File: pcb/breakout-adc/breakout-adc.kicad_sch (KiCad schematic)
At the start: 26 parts, among them J1 Screw_Terminal_01x04, J10 Conn_01x01_Pin, J11 Conn_01x12_Pin, J12 Conn_01x12_Pin, J13 Conn_01x01_Pin, J14 Conn_01x01_Pin, J15 FX18-120P-0.8SV20, J16 Conn_01x01_Pin, J17 Conn_01x01_Pin, J18 Conn_01x01_Pin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

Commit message: [adc][pcb] add colored keystone tp fp and models
Note: these need to have their footprints and models fixed
as they get used. I only did the ones on this board, even
though I downloaded and committed all the colors.
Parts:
- J7: footprint TestPoint:TestPoint_Keystone_5000-5004_Miniature -> keystone:KEYSTONE_5000
- J8: footprint TestPoint:TestPoint_Keystone_5000-5004_Miniature -> keystone:KEYSTONE_5116
- J9: footprint TestPoint:TestPoint_Keystone_5000-5004_Miniature -> keystone:KEYSTONE_5117
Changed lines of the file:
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@@
 			)
 		)
-		(property "Footprint" "TestPoint:TestPoint_Keystone_5000-5004_Miniature"
+		(property "Footprint" "keystone:KEYSTONE_5117"
 			(at 298.45 92.71 0)
 			(effects
@@
 			)
 		)
-		(property "Footprint" "TestPoint:TestPoint_Keystone_5000-5004_Miniature"
+		(property "Footprint" "keystone:KEYSTONE_5000"
 			(at 298.45 85.09 0)
 			(effects
@@
 			)
 		)
-		(property "Footprint" "TestPoint:TestPoint_Keystone_5000-5004_Miniature"
+		(property "Footprint" "keystone:KEYSTONE_5116"
 			(at 298.45 88.9 0)
 			(effects

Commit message: [adc][pcb] move the 3v3 and gnd tp to the edge
This will (probably) allow for grabbers to connect
to the through holes even if the tp isn't soldered in.
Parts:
- J10, J14, J16, J17, J18, J5, J6: footprint TestPoint:TestPoint_Keystone_5000-5004_Miniature -> keystone:KEYSTONE_5001
- J13: footprint TestPoint:TestPoint_Keystone_5000-5004_Miniature -> keystone:KEYSTONE_5000
- J3, J4: footprint TestPoint:TestPoint_Keystone_5000-5004_Miniature -> keystone:KEYSTONE_5002
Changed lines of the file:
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@@
 			)
 		)
-		(property "Footprint" "TestPoint:TestPoint_Keystone_5000-5004_Miniature"
+		(property "Footprint" "keystone:KEYSTONE_5001"
 			(at 392.43 63.5 0)
 			(effects
@@
 			)
 		)
-		(property "Footprint" "TestPoint:TestPoint_Keystone_5000-5004_Miniature"
+		(property "Footprint" "keystone:KEYSTONE_5002"
 			(at 298.45 58.42 0)
 			(effects
@@
 			)
 		)
-		(property "Footprint" "TestPoint:TestPoint_Keystone_5000-5004_Miniature"
+		(property "Footprint" "keystone:KEYSTONE_5002"
 			(at 298.45 55.88 0)
 			(effects
@@
 			)
 		)
-		(property "Footprint" "TestPoint:TestPoint_Keystone_5000-5004_Miniature"
+		(property "Footprint" "keystone:KEYSTONE_5001"
 			(at 298.45 96.52 0)
 			(effects
@@
 			)
 		)
-		(property "Footprint" "TestPoint:TestPoint_Keystone_5000-5004_Miniature"
+		(property "Footprint" "keystone:KEYSTONE_5001"
 			(at 392.43 90.17 0)
 			(effects
@@
 			)
 		)
-		(property "Footprint" "TestPoint:TestPoint_Keystone_5000-5004_Miniature"
+		(property "Footprint" "keystone:KEYSTONE_5001"
 			(at 392.43 85.09 0)
 			(effects
@@
 			)
 		)
-		(property "Footprint" "TestPoint:TestPoint_Keystone_5000-5004_Miniature"
+		(property "Footprint" "keystone:KEYSTONE_5001"
 			(at 392.43 87.63 0)
 			(effects
@@
 			)
 		)
-		(property "Footprint" "TestPoint:TestPoint_Keystone_5000-5004_Miniature"
+		(property "Footprint" "keystone:KEYSTONE_5001"
 			(at 298.45 63.5 0)
 			(effects
@@
 			)
 		)
-		(property "Footprint" "TestPoint:TestPoint_Keystone_5000-5004_Miniature"
+		(property "Footprint" "keystone:KEYSTONE_5000"
 			(at 392.43 60.96 0)
 			(effects
@@
 			)
 		)
-		(property "Footprint" "TestPoint:TestPoint_Keystone_5000-5004_Miniature"
+		(property "Footprint" "keystone:KEYSTONE_5001"
 			(at 298.45 60.96 0)
 			(effects

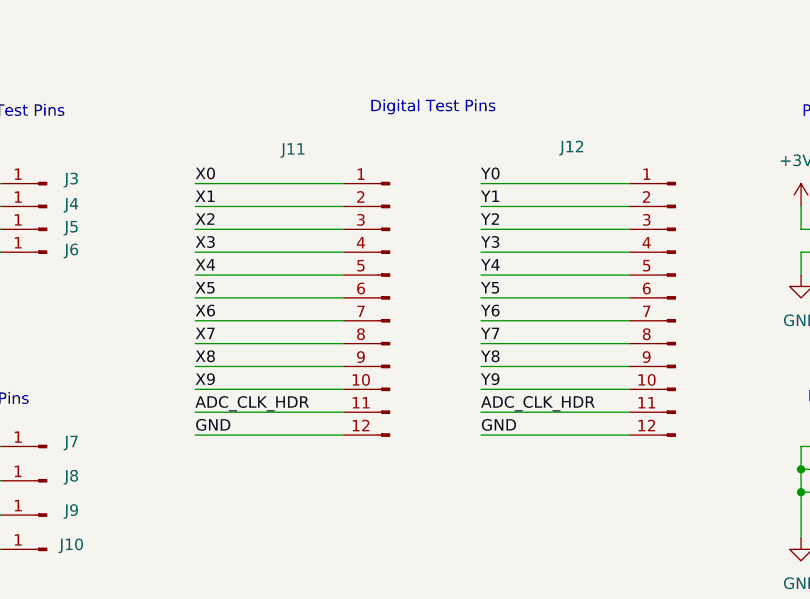
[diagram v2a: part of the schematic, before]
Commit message: [adc][pcb] routed data to buffers
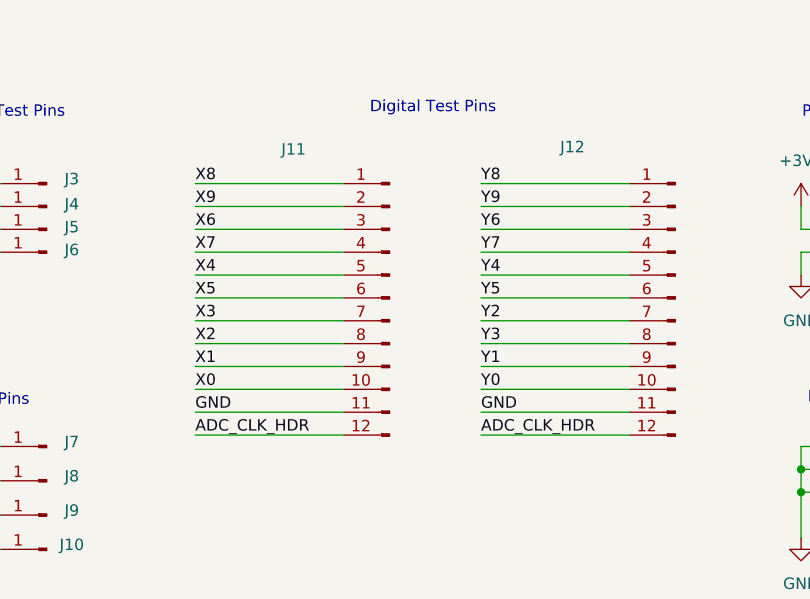
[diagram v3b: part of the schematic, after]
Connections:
- net ADC_CLK_HDR: now also J11.12 (Pin_12), J12.12 (Pin_12); no longer J11.11 (Pin_11), J12.11 (Pin_11)
- net GND: now also J11.11 (Pin_11), J12.11 (Pin_11); no longer J11.12 (Pin_12), J12.12 (Pin_12)
- net X0: now also J11.10 (Pin_10); no longer J11.1 (Pin_1)
- net X1: now also J11.9 (Pin_9); no longer J11.2 (Pin_2)
- net X2: now also J11.8 (Pin_8); no longer J11.3 (Pin_3)
- net X3: now also J11.7 (Pin_7); no longer J11.4 (Pin_4)
- net X6: now also J11.3 (Pin_3); no longer J11.7 (Pin_7)
- net X7: now also J11.4 (Pin_4); no longer J11.8 (Pin_8)
- net X8: now also J11.1 (Pin_1); no longer J11.9 (Pin_9)
- net X9: now also J11.2 (Pin_2); no longer J11.10 (Pin_10)
- net Y0: now also J12.10 (Pin_10); no longer J12.1 (Pin_1)
- net Y1: now also J12.9 (Pin_9); no longer J12.2 (Pin_2)
- net Y2: now also J12.7 (Pin_7); no longer J12.3 (Pin_3)
- net Y3: now also J12.8 (Pin_8); no longer J12.4 (Pin_4)
- net Y6: now also J12.3 (Pin_3); no longer J12.7 (Pin_7)
- net Y7: now also J12.4 (Pin_4); no longer J12.8 (Pin_8)
- net Y8: now also J12.1 (Pin_1); no longer J12.9 (Pin_9)
- net Y9: now also J12.2 (Pin_2); no longer J12.10 (Pin_10)
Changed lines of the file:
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@@
 	)
 	(label "Y0"
-		(at 346.71 55.88 0)
+		(at 346.71 78.74 0)
 		(fields_autoplaced yes)
 		(effects
@@
 	)
 	(label "GND"
-		(at 314.96 83.82 0)
+		(at 314.96 81.28 0)
 		(fields_autoplaced yes)
 		(effects
@@
 	)
 	(label "Y8"
-		(at 346.71 76.2 0)
+		(at 346.71 55.88 0)
 		(fields_autoplaced yes)
 		(effects
@@
 	)
 	(label "Y7"
+		(at 346.71 63.5 0)
+		(fields_autoplaced yes)
+		(effects
+			(font
+				(size 1.27 1.27)
+			)
+			(justify left bottom)
+		)
+	)
+	(label "GND"
+		(at 129.54 228.6 180)
+		(fields_autoplaced yes)
+		(effects
+			(font
+				(size 1.27 1.27)
+			)
+			(justify right bottom)
+		)
+	)
+	(label "Y3"
 		(at 346.71 73.66 0)
-		(fields_autoplaced yes)
-		(effects
-			(font
-				(size 1.27 1.27)
-			)
-			(justify left bottom)
-		)
-	)
-	(label "GND"
-		(at 129.54 228.6 180)
-		(fields_autoplaced yes)
-		(effects
-			(font
-				(size 1.27 1.27)
-			)
-			(justify right bottom)
-		)
-	)
-	(label "Y3"
-		(at 346.71 63.5 0)
 		(fields_autoplaced yes)
 		(effects
@@
 	)
 	(label "Y6"
-		(at 346.71 71.12 0)
+		(at 346.71 60.96 0)
 		(fields_autoplaced yes)
 		(effects
@@
 	)
 	(label "Y9"
-		(at 346.71 78.74 0)
+		(at 346.71 58.42 0)
 		(fields_autoplaced yes)
 		(effects
@@
 	)
 	(label "ADC_CLK_HDR"
-		(at 346.71 81.28 0)
+		(at 346.71 83.82 0)
 		(fields_autoplaced yes)
 		(effects
@@
 	)
 	(label "X1"
-		(at 314.96 58.42 0)
+		(at 314.96 76.2 0)
 		(fields_autoplaced yes)
 		(effects
@@
 	)
 	(label "Y1"
-		(at 346.71 58.42 0)
+		(at 346.71 76.2 0)
 		(fields_autoplaced yes)
 		(effects
@@
 	)
 	(label "X8"
-		(at 314.96 76.2 0)
+		(at 314.96 55.88 0)
 		(fields_autoplaced yes)
 		(effects
@@
 	)
 	(label "X0"
-		(at 314.96 55.88 0)
+		(at 314.96 78.74 0)
 		(fields_autoplaced yes)
 		(effects
@@
 	)
 	(label "ADC_CLK_HDR"
-		(at 314.96 81.28 0)
+		(at 314.96 83.82 0)
 		(fields_autoplaced yes)
 		(effects
@@
 	)
 	(label "X2"
-		(at 314.96 60.96 0)
+		(at 314.96 73.66 0)
 		(fields_autoplaced yes)
 		(effects
@@
 	)
 	(label "X3"
-		(at 314.96 63.5 0)
+		(at 314.96 71.12 0)
 		(fields_autoplaced yes)
 		(effects
@@
 	)
 	(label "GND"
-		(at 346.71 83.82 0)
+		(at 346.71 81.28 0)
 		(fields_autoplaced yes)
 		(effects
@@
 	)
 	(label "X9"
-		(at 314.96 78.74 0)
+		(at 314.96 58.42 0)
 		(fields_autoplaced yes)
 		(effects
@@
 	)
 	(label "Y2"
-		(at 346.71 60.96 0)
+		(at 346.71 71.12 0)
 		(fields_autoplaced yes)
 		(effects
@@
 	)
 	(label "X7"
-		(at 314.96 73.66 0)
+		(at 314.96 63.5 0)
 		(fields_autoplaced yes)
 		(effects
@@
 	)
 	(label "X6"
-		(at 314.96 71.12 0)
-		(fields_autoplaced yes)
-		(effects
+		(at 314.96 60.96 0)
+		(fields_autoplaced yes)
+		(effects

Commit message: [pcb] prep work for FX18-120P footprint fix
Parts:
- J15: footprint custom:CUSTOM_FX_120S-0.8SH20 -> CONN_120P-0.8SV20
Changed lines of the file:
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@@
 	)
 	(symbol
+		(lib_name "FX18-120P-0.8SV20_1")
 		(lib_id "FX18-120P-0-8SV20:FX18-120P-0.8SV20")
 		(at 52.07 142.24 0)
@@
 			)
 		)
-		(property "Footprint" "custom:CUSTOM_FX_120S-0.8SH20"
+		(property "Footprint" "CONN_120P-0.8SV20"
 			(at 52.07 142.24 0)
 			(effects
@@
 			)
 		)
-		(property "Datasheet" "FX18-120P-0.8SV20"
+		(property "Datasheet" "https://www.hirose.com/en/product/document?clcode=CL0579-0020-7-00&productname=FX18-120P-0.8SV&series=FX18&documenttype=2DDrawing&lang=en&documentid=0000920405"
 			(at 52.07 142.24 0)
 			(effects

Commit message: [pcb] add FX18-120P footprint and update pcbs
and a few adc fixes, including a key resistor fix
(the op amp for Y had a copy paste error from X
on the positive Rg)
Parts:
- J15: footprint custom:CUSTOM_FX_120S-0.8SH20 -> custom:CUSTOM_FX_120P-0.8SH20
- J15: footprint CONN_120P-0.8SV20 -> custom:CUSTOM_FX_120P-0.8SH20
- U8, U9: footprint D1213A:SOT-363_DIO -> SOT-363_DIO
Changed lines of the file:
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@@
 			)
 		)
-		(property "Footprint" "custom:CUSTOM_FX_120S-0.8SH20"
+		(property "Footprint" "custom:CUSTOM_FX_120P-0.8SH20"
 			(at 86.36 142.24 0)
 			(effects
@@
 			)
 		)
-		(property "Datasheet" "FX18-120P-0.8SV20"
+		(property "Datasheet" "https://www.hirose.com/en/product/document?clcode=CL0579-0020-7-00&productname=FX18-120P-0.8SV&series=FX18&documenttype=2DDrawing&lang=en&documentid=0000920405"
 			(at 86.36 142.24 0)
 			(effects
@@
 	)
 	(symbol
-		(lib_name "D1213A-04S-7_1")
 		(lib_id "D1213A-04S:D1213A-04S-7")
 		(at 111.76 46.99 0)
@@
 			)
 		)
-		(property "Footprint" "D1213A:SOT-363_DIO"
+		(property "Footprint" "SOT-363_DIO"
 			(at 111.76 46.99 0)
 			(effects
@@
 			)
 		)
-		(property "Datasheet" "https://www.diodes.com/assets/Datasheets/D1213A-04S.pdf"
+		(property "Datasheet" "D1213A-04S-7"
 			(at 111.76 46.99 0)
 			(effects
@@
 			)
 		)
-		(property "Footprint" "custom:CUSTOM_FX_120S-0.8SH20"
+		(property "Footprint" "custom:CUSTOM_FX_120P-0.8SH20"
 			(at 123.19 142.24 0)
 			(effects
@@
 			)
 		)
-		(property "Datasheet" "FX18-120P-0.8SV20"
+		(property "Datasheet" "https://www.hirose.com/en/product/document?clcode=CL0579-0020-7-00&productname=FX18-120P-0.8SV&series=FX18&documenttype=2DDrawing&lang=en&documentid=0000920405"
 			(at 123.19 142.24 0)
 			(effects
@@
 			)
 		)
-		(property "Footprint" "D1213A:SOT-363_DIO"
+		(property "Footprint" "SOT-363_DIO"
 			(at 111.76 97.79 0)
 			(effects
@@
 			)
 		)
-		(property "Datasheet" "https://www.diodes.com/assets/Datasheets/D1213A-04S.pdf"
+		(property "Datasheet" "D1213A-04S-7"
 			(at 111.76 97.79 0)
 			(effects
@@
 	)
 	(symbol
-		(lib_name "FX18-120P-0.8SV20_1")
 		(lib_id "FX18-120P-0-8SV20:FX18-120P-0.8SV20")
 		(at 52.07 142.24 0)
@@
 			)
 		)
-		(property "Footprint" "CONN_120P-0.8SV20"
+		(property "Footprint" "custom:CUSTOM_FX_120P-0.8SH20"
 			(at 52.07 142.24 0)
 			(effects

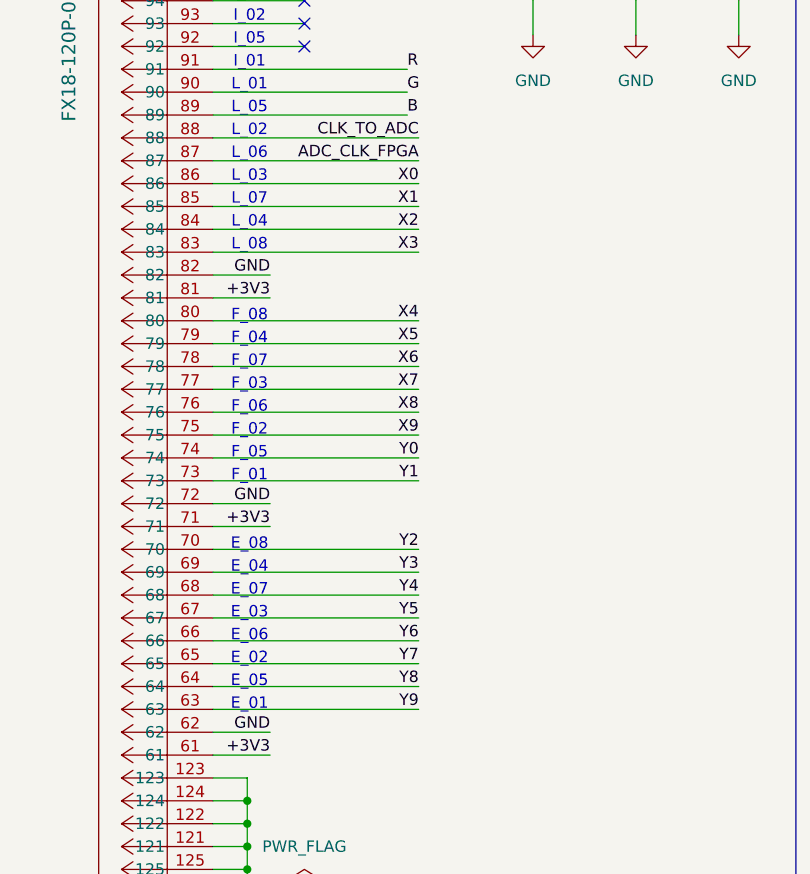
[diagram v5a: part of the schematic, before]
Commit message: [adc][pcb] data routed to FX conn
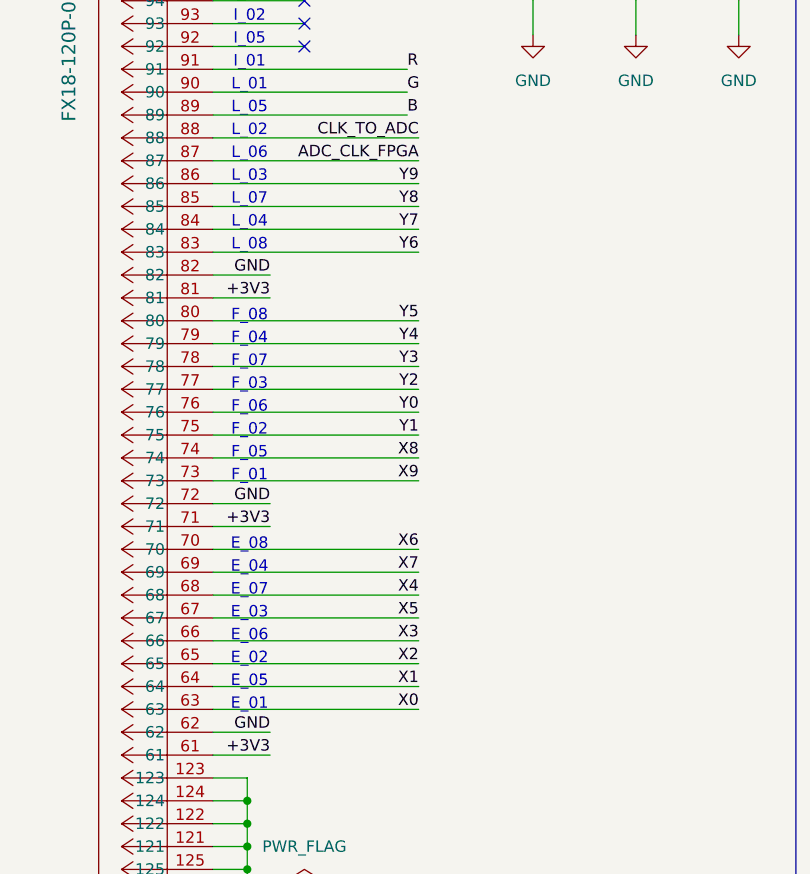
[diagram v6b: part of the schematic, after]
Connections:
- net X0: now also J15.63; no longer J15.86
- net X1: now also J15.64; no longer J15.85
- net X2: now also J15.65; no longer J15.84
- net X3: now also J15.66; no longer J15.83
- net X4: now also J15.68; no longer J15.80
- net X5: now also J15.67; no longer J15.79
- net X6: now also J15.70; no longer J15.78
- net X7: now also J15.69; no longer J15.77
- net X8: now also J15.74; no longer J15.76
- net X9: now also J15.73; no longer J15.75
- net Y0: now also J15.76; no longer J15.74
- net Y1: now also J15.75; no longer J15.73
- net Y2: now also J15.77; no longer J15.70
- net Y3: now also J15.78; no longer J15.69
- net Y4: now also J15.79; no longer J15.68
- net Y5: now also J15.80; no longer J15.67
- net Y6: now also J15.83; no longer J15.66
- net Y7: now also J15.84; no longer J15.65
- net Y8: now also J15.85; no longer J15.64
- net Y9: now also J15.86; no longer J15.63
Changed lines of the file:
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@@
 	)
 	(label "Y4"
-		(at 146.05 213.36 180)
+		(at 146.05 185.42 180)
 		(fields_autoplaced yes)
 		(effects
@@
 	)
 	(label "Y7"
-		(at 146.05 220.98 180)
+		(at 146.05 172.72 180)
 		(fields_autoplaced yes)
 		(effects
@@
 	)
 	(label "Y3"
-		(at 146.05 210.82 180)
+		(at 146.05 187.96 180)
 		(fields_autoplaced yes)
 		(effects
@@
 	)
 	(label "X8"
-		(at 146.05 193.04 180)
+		(at 146.05 198.12 180)
 		(fields_autoplaced yes)
 		(effects
@@
 	)
 	(label "Y5"
-		(at 146.05 215.9 180)
+		(at 146.05 182.88 180)
 		(fields_autoplaced yes)
 		(effects
@@
 	)
 	(label "X3"
-		(at 146.05 175.26 180)
+		(at 146.05 218.44 180)
 		(fields_autoplaced yes)
 		(effects
@@
 	)
 	(label "Y1"
-		(at 146.05 200.66 180)
+		(at 146.05 195.58 180)
 		(fields_autoplaced yes)
 		(effects
@@
 	)
 	(label "X7"
+		(at 146.05 210.82 180)
+		(fields_autoplaced yes)
+		(effects
+			(font
+				(size 1.27 1.27)
+			)
+			(justify right bottom)
+		)
+	)
+	(label "Y2"
 		(at 146.05 190.5 180)
 		(fields_autoplaced yes)
@@
 		)
 	)
-	(label "Y2"
-		(at 146.05 208.28 180)
-		(fields_autoplaced yes)
-		(effects
-			(font
-				(size 1.27 1.27)
-			)
-			(justify right bottom)
-		)
-	)
 	(label "+3V3"
 		(at 62.23 167.64 180)
@@
 	)
 	(label "X9"
-		(at 146.05 195.58 180)
+		(at 146.05 200.66 180)
 		(fields_autoplaced yes)
 		(effects
@@
 	)
 	(label "Y9"
-		(at 146.05 226.06 180)
+		(at 146.05 167.64 180)
 		(fields_autoplaced yes)
 		(effects
@@
 	)
 	(label "X2"
-		(at 146.05 172.72 180)
+		(at 146.05 220.98 180)
 		(fields_autoplaced yes)
 		(effects
@@
 	)
 	(label "Y8"
-		(at 146.05 223.52 180)
+		(at 146.05 170.18 180)
 		(fields_autoplaced yes)
 		(effects
@@
 	)
 	(label "Y0"
-		(at 146.05 198.12 180)
+		(at 146.05 193.04 180)
 		(fields_autoplaced yes)
 		(effects
@@
 	)
 	(label "X4"
-		(at 146.05 182.88 180)
+		(at 146.05 213.36 180)
 		(fields_autoplaced yes)
 		(effects
@@
 	)
 	(label "X1"
-		(at 146.05 170.18 180)
+		(at 146.05 223.52 180)
 		(fields_autoplaced yes)
 		(effects
@@
 	)
 	(label "X6"
-		(at 146.05 187.96 180)
+		(at 146.05 208.28 180)
 		(fields_autoplaced yes)
 		(effects
@@
 	)
 	(label "X5"
-		(at 146.05 185.42 180)
+		(at 146.05 215.9 180)
 		(fields_autoplaced yes)
 		(effects
@@
 	)
 	(label "X0"
-		(at 146.05 167.64 180)
+		(at 146.05 226.06 180)
 		(fields_autoplaced yes)
 		(effects
@@
 	)
 	(label "Y6"
-		(at 146.05 218.44 180)
-		(fields_autoplaced yes)
-		(effects
+		(at 146.05 175.26 180)
+		(fields_autoplaced yes)
+		(effects

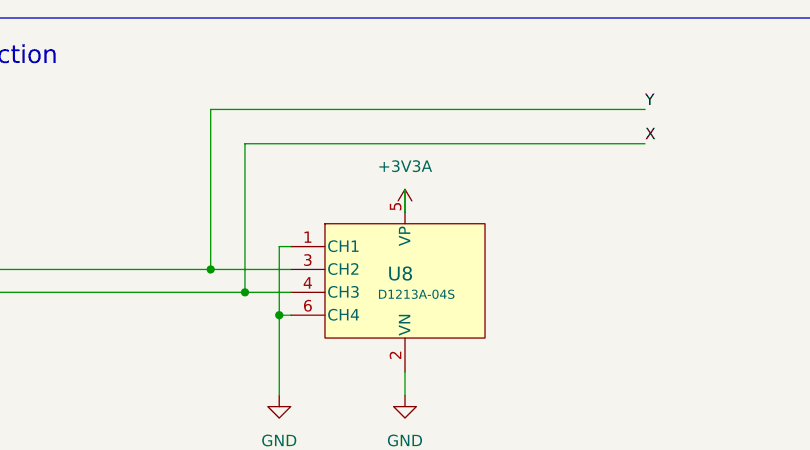
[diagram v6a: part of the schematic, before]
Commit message: [adc][pcb] fully routed
needs some return trace cleanup, return path checks,
gnd/power plane touchups, and some drc fixes/tweaks.
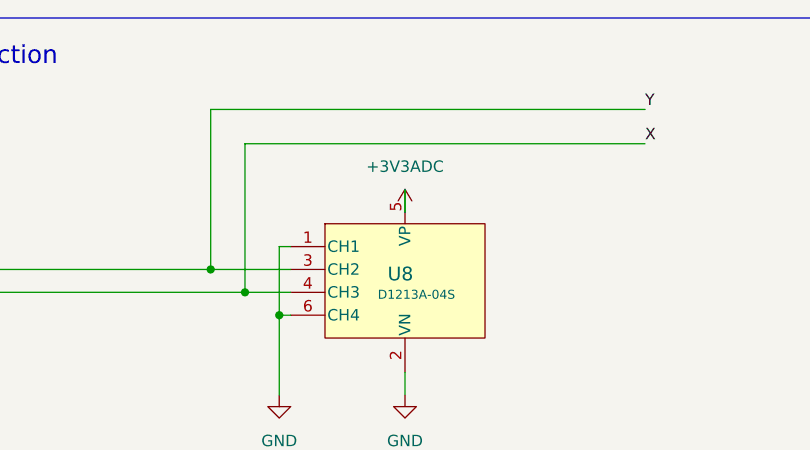
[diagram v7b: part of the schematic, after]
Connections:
- net +3V3A renamed +3V3ADC
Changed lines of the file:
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@@
 			)
 		)
-		(property "Value" "+3V3A"
+		(property "Value" "+3V3ADC"
 			(at 111.76 34.29 0)
 			(effects

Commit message: [adc][pcb] relink footprints to fix drc issue
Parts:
- U8, U9: footprint SOT-363_DIO -> D1213A:SOT-363_DIO
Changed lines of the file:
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@@
 			)
 		)
-		(property "Footprint" "SOT-363_DIO"
+		(property "Footprint" "D1213A:SOT-363_DIO"
 			(at 111.76 46.99 0)
 			(effects
@@
 			)
 		)
-		(property "Footprint" "SOT-363_DIO"
+		(property "Footprint" "D1213A:SOT-363_DIO"
 			(at 111.76 97.79 0)
 			(effects
